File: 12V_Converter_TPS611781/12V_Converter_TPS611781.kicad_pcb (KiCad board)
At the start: 2 copper layers, 38.7 x 27.2 mm, 23 parts, among them M1 IQE050N08NM5CGSC, U1 LM51561HPWPR

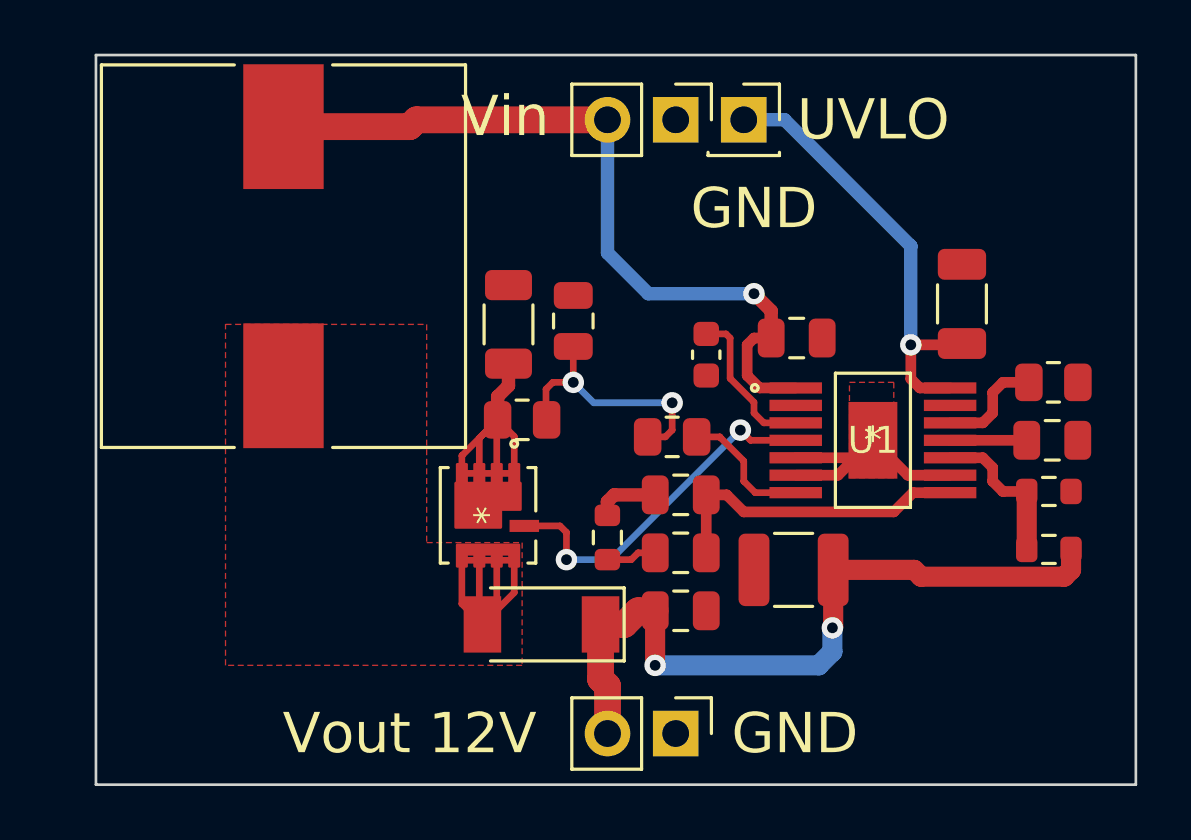
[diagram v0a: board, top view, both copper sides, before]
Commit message: made things better :)
moved current sense resistor closer to the spot that senses the current
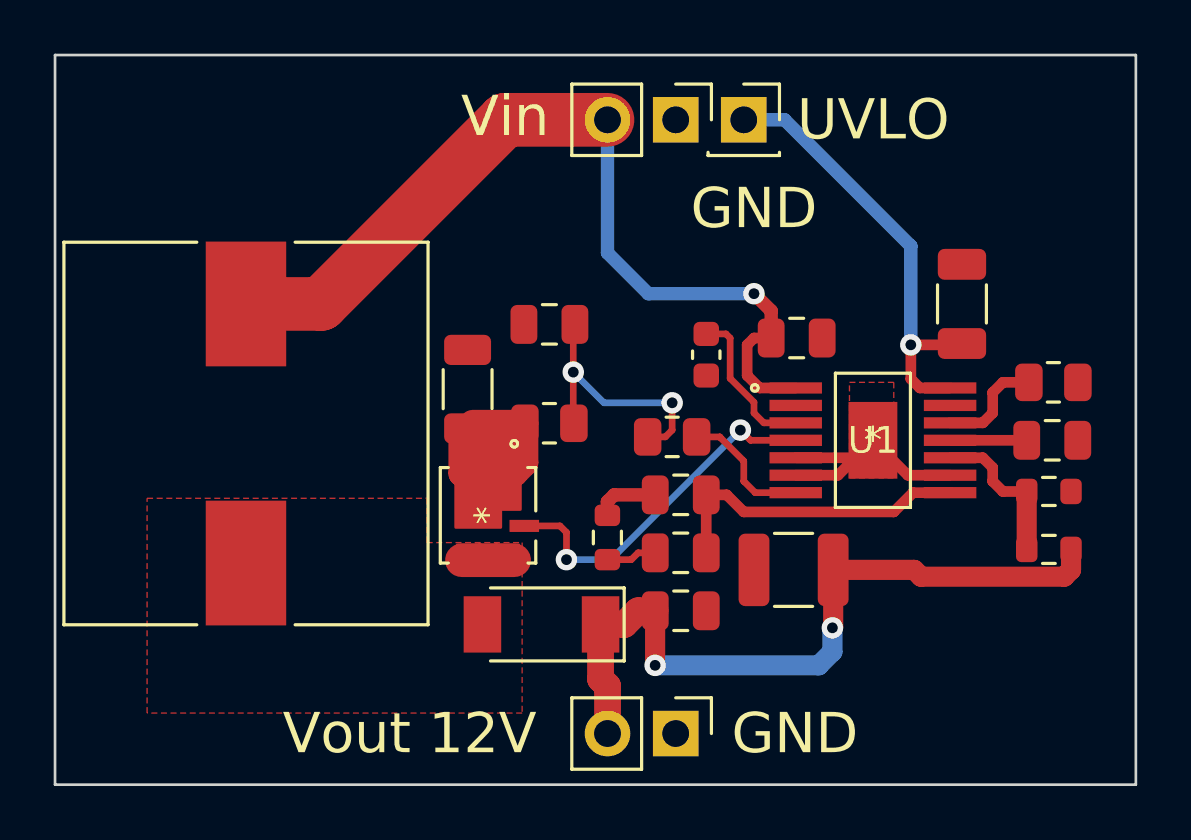
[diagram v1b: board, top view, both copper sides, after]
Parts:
- moved L1 6.75 mm to (63.4, 109.6)
- moved Rcs2 2.85 mm to (71.6, 108.0)
- moved Rcs1 1.02 mm to (74.7, 109.2)
- moved Ccs1 0.90 mm to (74.7, 105.5), turned to 180 degrees
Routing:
- net Net-(D1-Pad2): track 12.6 -> 1.95 mm
- net Vin: track 29.3 -> 33.4 mm
- net Net-(Rcs1-Pad2): track 13.3 -> 14.8 mm
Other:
- board size 38.7 x 27.2 mm -> 40.3 x 27.2 mm

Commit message: reduced switching loop area
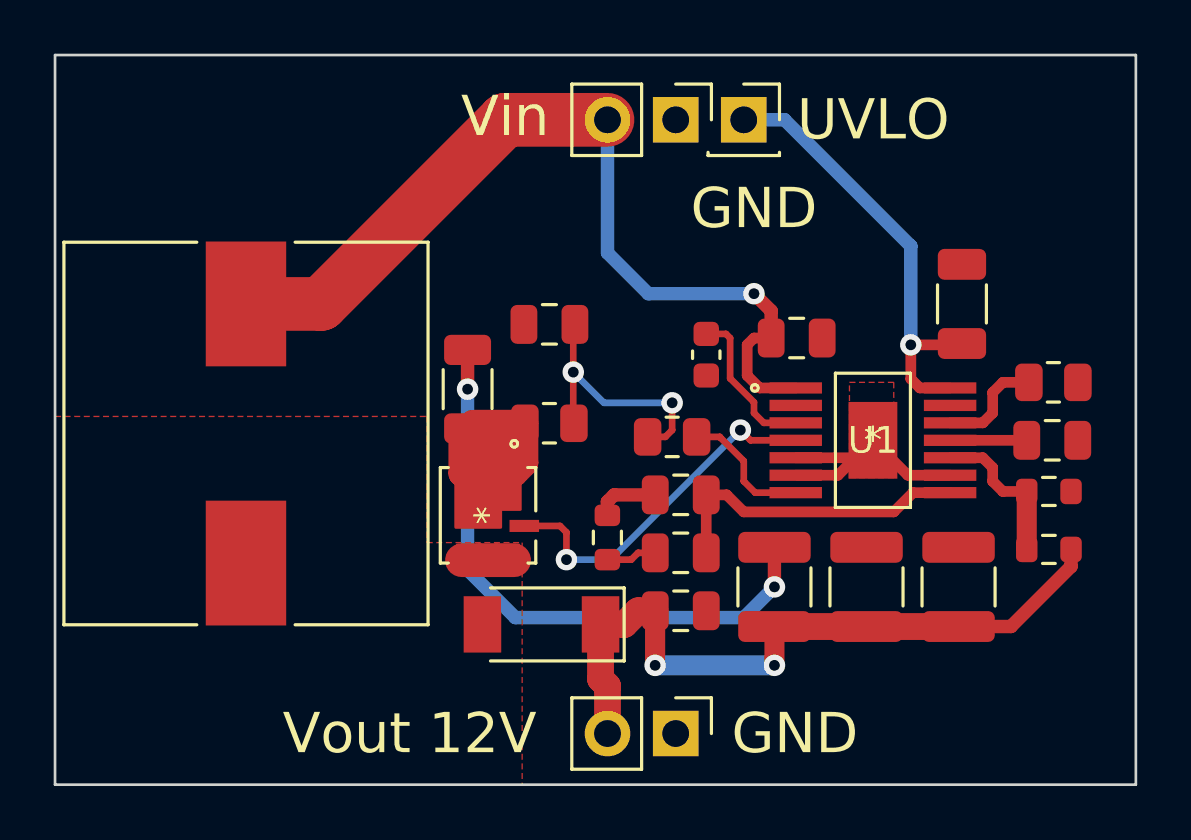
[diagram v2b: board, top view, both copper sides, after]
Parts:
- added Cout2: 22uF, Capacitor_SMD:C_1210_3225Metric, F.Cu at (89.9, 115.3)
- added Cout3: 22uF, Capacitor_SMD:C_1210_3225Metric, F.Cu at (86.5, 115.3)
- moved Cout1 0.95 mm to (83.1, 115.3), turned to 90 degrees
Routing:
- net GND: track 12.4 -> 34.7 mm, vias 0 -> 2
- net Vout: track 28.2 -> 27.0 mm

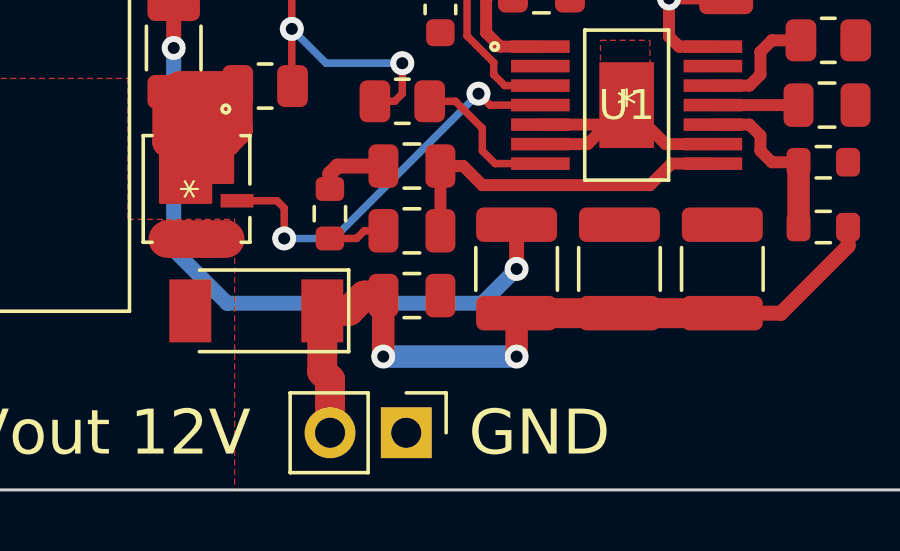
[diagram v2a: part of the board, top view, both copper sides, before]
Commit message: shifted traces
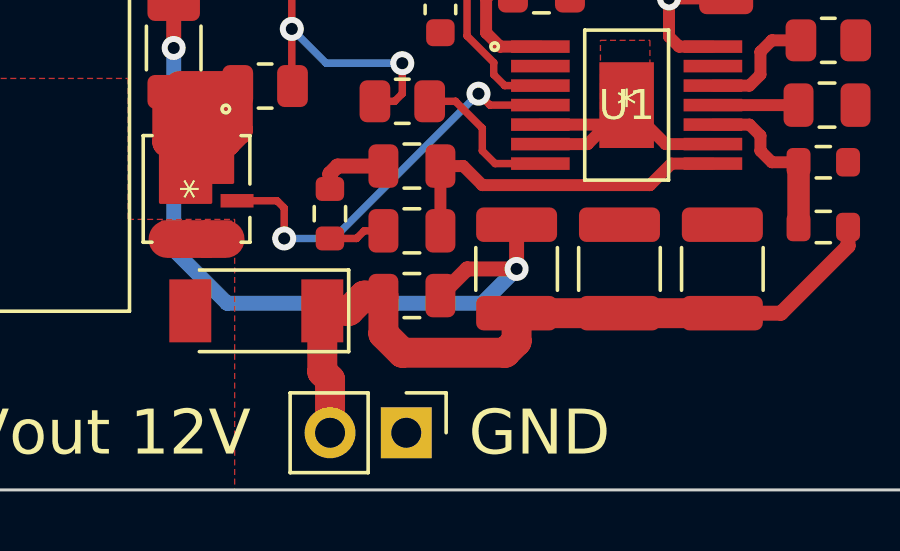
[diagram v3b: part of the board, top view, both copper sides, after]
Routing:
- net GND: track 34.7 -> 37.6 mm
- net Vout: track 27.0 -> 26.1 mm, vias 2 -> 0
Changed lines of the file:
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@@
   (segment (start 83.850566 111.155) (end 85.42595 111.155) (width 0.4) (layer "F.Cu") (net 2))
   (segment (start 78.618 111.887) (end 77.089 111.887) (width 0.5) (layer "F.Cu") (net 2))
+  (segment (start 81.407 115.316) (end 83.058 115.316) (width 0.5) (layer "F.Cu") (net 2))
+  (segment (start 80.518 116.205) (end 81.407 115.316) (width 0.5) (layer "F.Cu") (net 2))
   (segment (start 89.601334 111.155) (end 88.02595 111.155) (width 0.4) (layer "F.Cu") (net 2))
   (segment (start 83.850566 110.505001) (end 86.075949 110.505001) (width 0.4) (layer "F.Cu") (net 2))
@@
   (segment (start 94.106 114.555) (end 91.87 116.791) (width 0.5) (layer "F.Cu") (net 6))
   (segment (start 94.106 113.919) (end 94.106 114.555) (width 0.5) (layer "F.Cu") (net 6))
-  (segment (start 78.613 116.21) (end 78.618 116.205) (width 0.75) (layer "F.Cu") (net 6))
+  (segment (start 79.248 118.11) (end 78.618 117.48) (width 1) (layer "F.Cu") (net 6))
+  (segment (start 83.058 117.729) (end 82.677 118.11) (width 1) (layer "F.Cu") (net 6))
   (segment (start 89.916 116.791) (end 86.487 116.791) (width 1) (layer "F.Cu") (net 6))
-  (segment (start 83.058 118.237) (end 83.058 116.791) (width 0.75) (layer "F.Cu") (net 6))
   (segment (start 86.487 116.791) (end 83.058 116.791) (width 1) (layer "F.Cu") (net 6))
+  (segment (start 78.618 117.48) (end 78.618 116.205) (width 1) (layer "F.Cu") (net 6))
   (segment (start 77.47 116.713) (end 76.581 116.713) (width 1) (layer "F.Cu") (net 6))
+  (segment (start 83.058 116.791) (end 83.058 117.729) (width 1) (layer "F.Cu") (net 6))
   (segment (start 76.581 118.745) (end 76.84 119.004) (width 1) (layer "F.Cu") (net 6))
   (segment (start 77.978 116.205) (end 77.47 116.713) (width 1) (layer "F.Cu") (net 6))
-  (segment (start 78.613 118.237) (end 78.613 116.21) (width 0.75) (layer "F.Cu") (net 6))
   (segment (start 91.87 116.791) (end 89.916 116.791) (width 0.5) (layer "F.Cu") (net 6))
   (segment (start 76.84 119.004) (end 76.84 120.777) (width 1) (layer "F.Cu") (net 6))
   (segment (start 78.618 116.205) (end 77.978 116.205) (width 1) (layer "F.Cu") (net 6))
-  (via (at 78.613 118.237) (size 0.8) (drill 0.4) (layers "F.Cu" "B.Cu") (net 6))
-  (via (at 83.058 118.237) (size 0.8) (drill 0.4) (layers "F.Cu" "B.Cu") (net 6))
-  (segment (start 78.613 118.237) (end 83.058 118.237) (width 0.75) (layer "B.Cu") (net 6))
+  (segment (start 82.677 118.11) (end 79.248 118.11) (width 1) (layer "F.Cu") (net 6))
   (segment (start 89.601334 109.855) (end 92.456 109.855) (width 0.4) (layer "F.Cu") (net 7))
   (segment (start 82.661999 109.204999) (end 82.296 108.839) (width 0.25) (layer "F.Cu") (net 8))

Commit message: made traces chonky
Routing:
- net GND: track 37.6 -> 44.4 mm
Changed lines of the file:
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@@
   (segment (start 77.089 111.887) (end 76.835 112.141) (width 0.5) (layer "F.Cu") (net 2))
   (segment (start 88.02595 111.155) (end 86.72595 109.855) (width 0.4) (layer "F.Cu") (net 2))
+  (segment (start 83.058 113.841) (end 86.487 113.841) (width 1) (layer "F.Cu") (net 2))
   (segment (start 83.850566 111.155) (end 85.42595 111.155) (width 0.4) (layer "F.Cu") (net 2))
   (segment (start 78.618 111.887) (end 77.089 111.887) (width 0.5) (layer "F.Cu") (net 2))
@@
   (segment (start 80.518 116.205) (end 81.407 115.316) (width 0.5) (layer "F.Cu") (net 2))
   (segment (start 89.601334 111.155) (end 88.02595 111.155) (width 0.4) (layer "F.Cu") (net 2))
+  (segment (start 86.487 113.841) (end 89.916 113.841) (width 1) (layer "F.Cu") (net 2))
   (segment (start 83.850566 110.505001) (end 86.075949 110.505001) (width 0.4) (layer "F.Cu") (net 2))
-  (segment (start 71.628 107.95) (end 71.628 106.4875) (width 0.5) (layer "F.Cu") (net 2))
-  (segment (start 83.058 113.841) (end 83.058 115.316) (width 0.5) (layer "F.Cu") (net 2))
+  (segment (start 71.628 107.95) (end 71.628 106.4875) (width 1) (layer "F.Cu") (net 2))
+  (segment (start 83.058 113.841) (end 83.058 115.316) (width 1) (layer "F.Cu") (net 2))
   (segment (start 86.075949 110.505001) (end 86.72595 109.855) (width 0.4) (layer "F.Cu") (net 2))
-  (via (at 71.628 107.95) (size 0.8) (drill 0.4) (layers "F.Cu" "B.Cu") (net 2))
-  (via (at 83.058 115.316) (size 0.8) (drill 0.4) (layers "F.Cu" "B.Cu") (net 2))
-  (segment (start 71.628 114.681) (end 71.628 107.95) (width 0.5) (layer "B.Cu") (net 2))
-  (segment (start 83.058 115.316) (end 81.915 116.459) (width 0.5) (layer "B.Cu") (net 2))
-  (segment (start 81.915 116.459) (end 73.406 116.459) (width 0.5) (layer "B.Cu") (net 2))
-  (segment (start 73.406 116.459) (end 71.628 114.681) (width 0.5) (layer "B.Cu") (net 2))
+  (via (at 71.628 107.95) (size 1) (drill 0.4) (layers "F.Cu" "B.Cu") (net 2))
+  (via (at 83.058 115.316) (size 1) (drill 0.4) (layers "F.Cu" "B.Cu") (net 2))
+  (segment (start 71.628 114.681) (end 71.628 107.95) (width 1) (layer "B.Cu") (net 2))
+  (segment (start 83.058 115.316) (end 81.915 116.459) (width 1) (layer "B.Cu") (net 2))
+  (segment (start 81.915 116.459) (end 73.406 116.459) (width 1) (layer "B.Cu") (net 2))
+  (segment (start 73.406 116.459) (end 71.628 114.681) (width 1) (layer "B.Cu") (net 2))
   (segment (start 77.978 114.046) (end 77.724 114.3) (width 0.25) (layer "F.Cu") (net 3))
   (segment (start 78.618 114.046) (end 77.978 114.046) (width 0.25) (layer "F.Cu") (net 3))

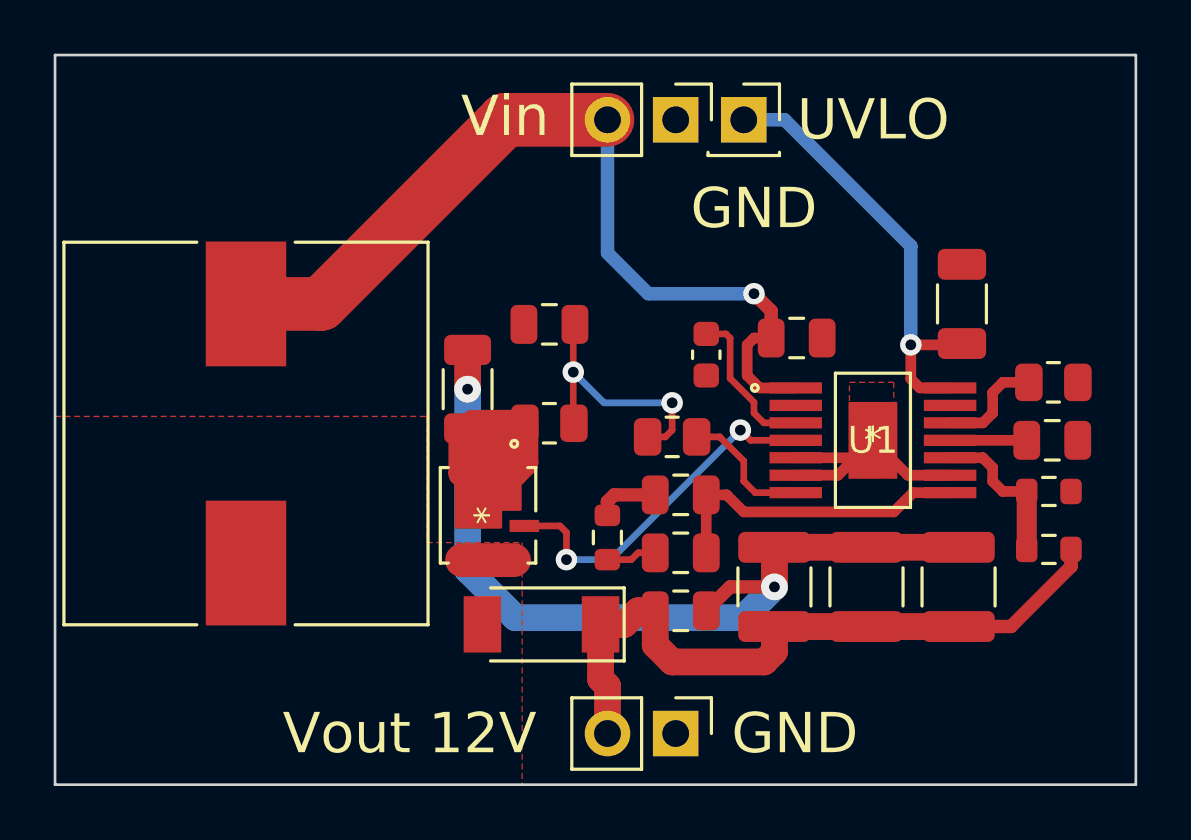
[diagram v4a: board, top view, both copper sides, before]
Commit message: made traces EXTRA CHONKY
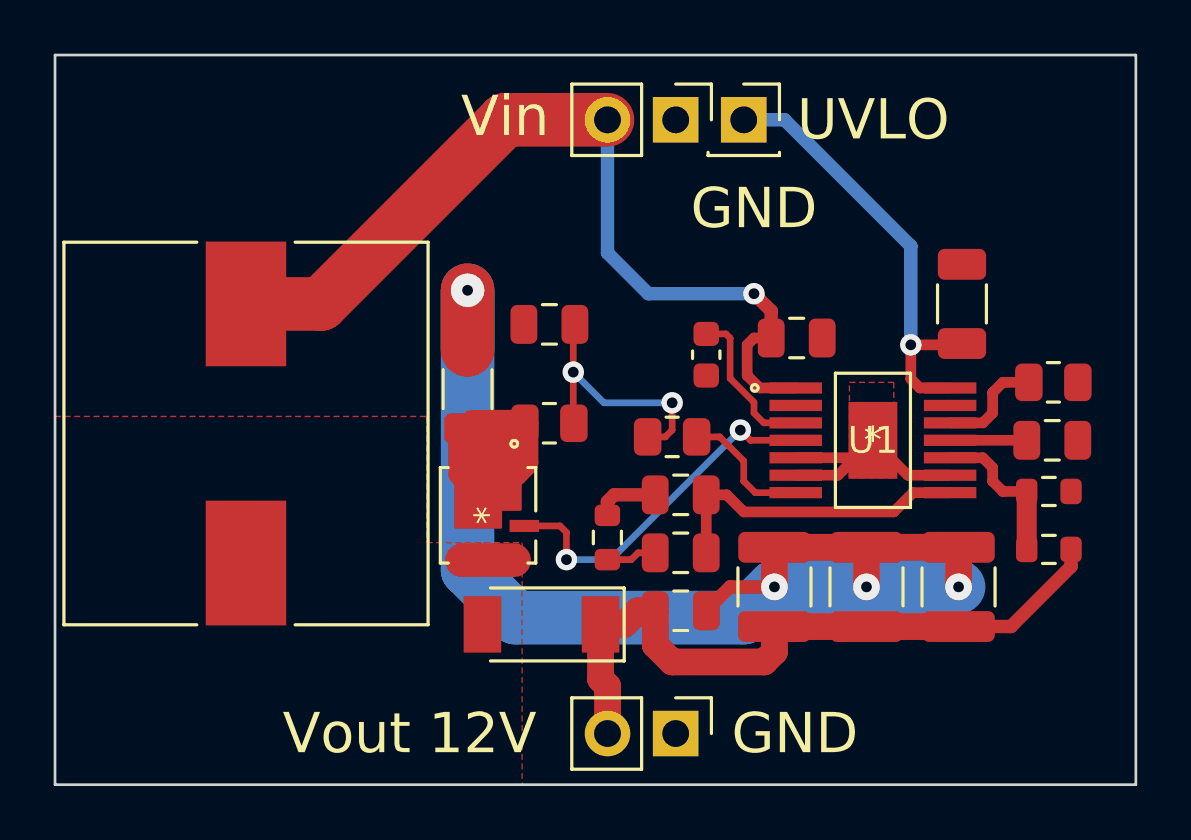
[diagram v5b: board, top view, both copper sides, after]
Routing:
- net GND: track 44.4 -> 58.7 mm, vias 2 -> 4
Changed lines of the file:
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@@
   (segment (start 82.296 104.394) (end 78.359 104.394) (width 0.5) (layer "B.Cu") (net 1))
   (segment (start 78.359 104.394) (end 76.84 102.875) (width 0.5) (layer "B.Cu") (net 1))
+  (segment (start 71.628 104.267) (end 71.628 106.4875) (width 2) (layer "F.Cu") (net 2))
   (segment (start 76.835 112.141) (end 76.835 112.65) (width 0.5) (layer "F.Cu") (net 2))
   (segment (start 85.42595 111.155) (end 86.72595 109.855) (width 0.4) (layer "F.Cu") (net 2))
@@
   (segment (start 83.850566 111.155) (end 85.42595 111.155) (width 0.4) (layer "F.Cu") (net 2))
   (segment (start 78.618 111.887) (end 77.089 111.887) (width 0.5) (layer "F.Cu") (net 2))
+  (segment (start 86.487 113.841) (end 86.487 115.316) (width 1) (layer "F.Cu") (net 2))
   (segment (start 81.407 115.316) (end 83.058 115.316) (width 0.5) (layer "F.Cu") (net 2))
   (segment (start 80.518 116.205) (end 81.407 115.316) (width 0.5) (layer "F.Cu") (net 2))
   (segment (start 89.601334 111.155) (end 88.02595 111.155) (width 0.4) (layer "F.Cu") (net 2))
   (segment (start 86.487 113.841) (end 89.916 113.841) (width 1) (layer "F.Cu") (net 2))
+  (segment (start 89.916 113.841) (end 89.916 115.316) (width 1) (layer "F.Cu") (net 2))
   (segment (start 83.850566 110.505001) (end 86.075949 110.505001) (width 0.4) (layer "F.Cu") (net 2))
-  (segment (start 71.628 107.95) (end 71.628 106.4875) (width 1) (layer "F.Cu") (net 2))
   (segment (start 83.058 113.841) (end 83.058 115.316) (width 1) (layer "F.Cu") (net 2))
   (segment (start 86.075949 110.505001) (end 86.72595 109.855) (width 0.4) (layer "F.Cu") (net 2))
-  (via (at 71.628 107.95) (size 1) (drill 0.4) (layers "F.Cu" "B.Cu") (net 2))
+  (via (at 71.628 104.267) (size 1.25) (drill 0.4) (layers "F.Cu" "B.Cu") (net 2))
   (via (at 83.058 115.316) (size 1) (drill 0.4) (layers "F.Cu" "B.Cu") (net 2))
-  (segment (start 71.628 114.681) (end 71.628 107.95) (width 1) (layer "B.Cu") (net 2))
-  (segment (start 83.058 115.316) (end 81.915 116.459) (width 1) (layer "B.Cu") (net 2))
-  (segment (start 81.915 116.459) (end 73.406 116.459) (width 1) (layer "B.Cu") (net 2))
-  (segment (start 73.406 116.459) (end 71.628 114.681) (width 1) (layer "B.Cu") (net 2))
+  (via (at 89.916 115.316) (size 1) (drill 0.4) (layers "F.Cu" "B.Cu") (net 2))
+  (via (at 86.487 115.316) (size 1) (drill 0.4) (layers "F.Cu" "B.Cu") (net 2))
+  (segment (start 71.628 114.681) (end 73.406 116.459) (width 2) (layer "B.Cu") (net 2))
+  (segment (start 71.628 104.267) (end 71.628 114.681) (width 2) (layer "B.Cu") (net 2))
+  (segment (start 81.915 116.459) (end 83.058 115.316) (width 2) (layer "B.Cu") (net 2))
+  (segment (start 83.058 115.316) (end 86.487 115.316) (width 2) (layer "B.Cu") (net 2))
+  (segment (start 86.487 115.316) (end 89.916 115.316) (width 2) (layer "B.Cu") (net 2))
+  (segment (start 73.406 116.459) (end 81.915 116.459) (width 2) (layer "B.Cu") (net 2))
   (segment (start 77.978 114.046) (end 77.724 114.3) (width 0.25) (layer "F.Cu") (net 3))
   (segment (start 78.618 114.046) (end 77.978 114.046) (width 0.25) (layer "F.Cu") (net 3))
